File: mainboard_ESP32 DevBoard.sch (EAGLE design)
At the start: 45 parts, among them IC1 OP-AMP-2-LONG, IC3 74HC08N, K1 AQH213, X1 JST-XH-02-PIN-LONG-PAD, X2 JST-XH-04-PIN-LONG-PAD, X3 1751248, X4 1751248, X5 JST-XH-04-PIN-LONG-PAD

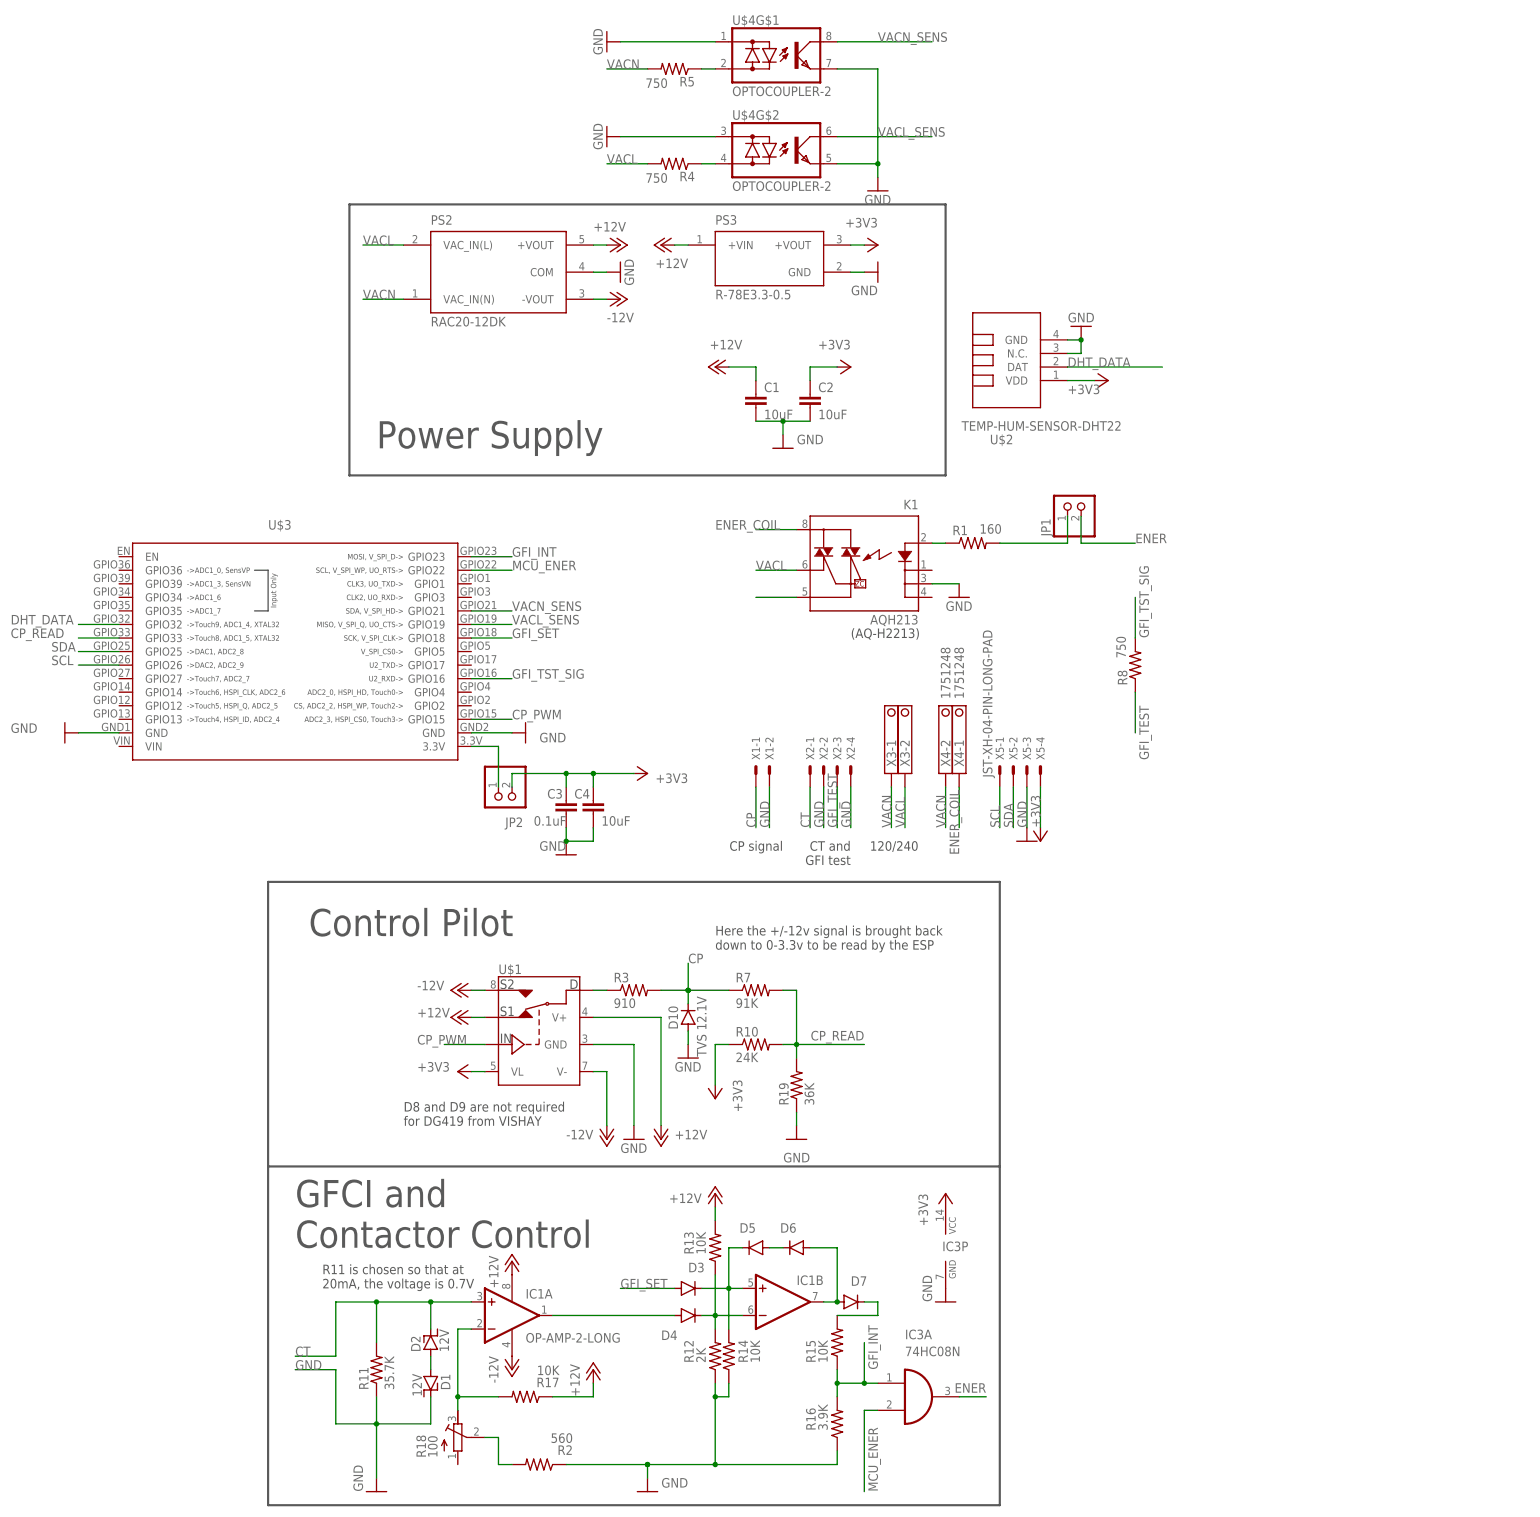
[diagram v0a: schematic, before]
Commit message: Added header for ac detection after contactor. Cleaned up schematic.
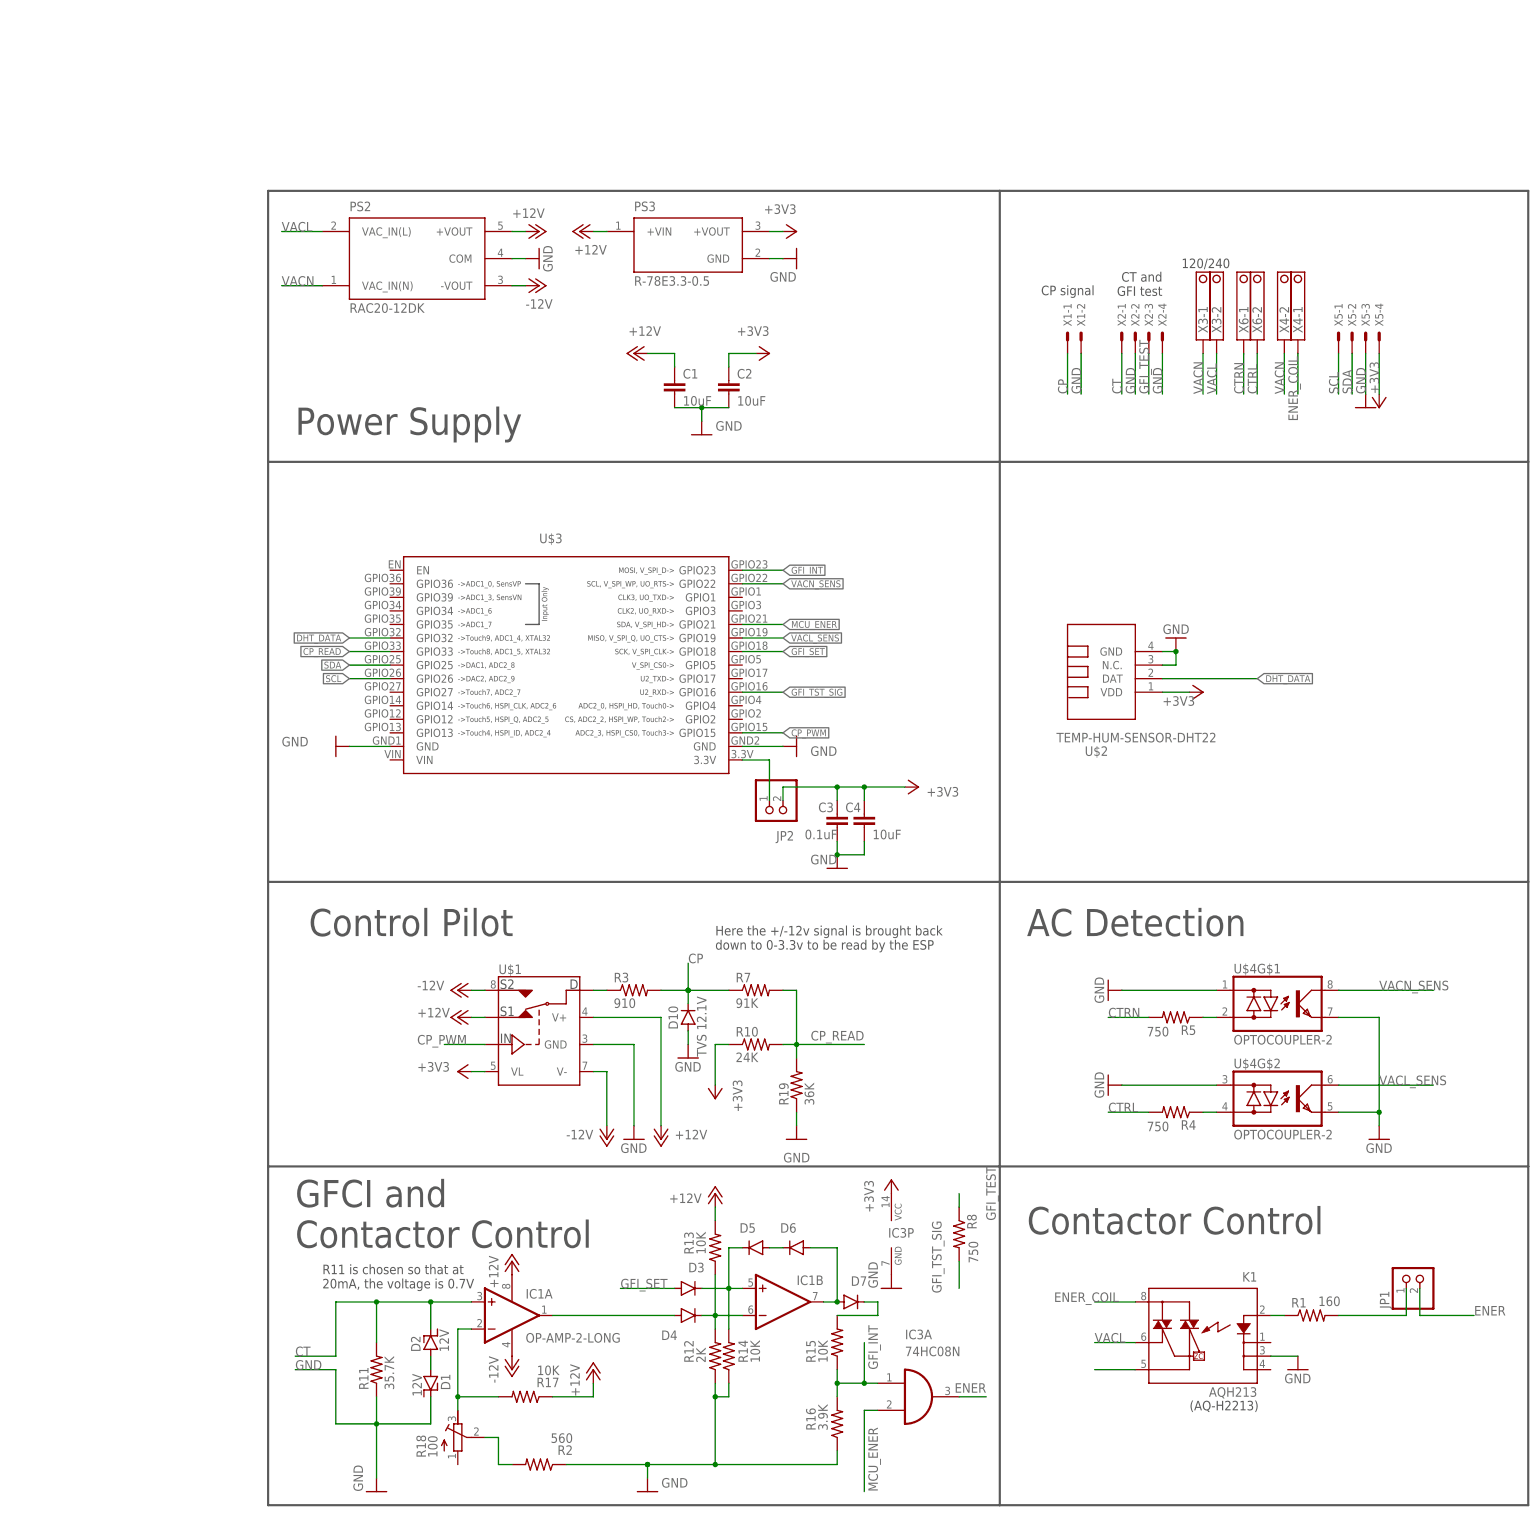
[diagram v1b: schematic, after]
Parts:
- added X6: 1751248, con-phoenix-350:1751248
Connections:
- new net CTRL: R4.2, X6-2.K
- new net CTRN: R5.2, X6-1.K
- net MCU_ENER: now also U$3.GPIO21; no longer U$3.GPIO22
- net VACL: no longer R4.2
- net VACN: no longer R5.2
- net VACN_SENS: now also U$3.GPIO22; no longer U$3.GPIO21
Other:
- note added: "AC Detection"
- note added: "Contactor Control"
- note removed: "D8 and D9 are not required for DG419 from VISHAY"
- moved on the sheet: C1, C2, C3, C4, IC3P, JP1, JP2, K1, PS2, PS3, R1, R4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
